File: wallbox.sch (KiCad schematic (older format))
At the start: 36 parts, among them J1 From Transformer, J2 To Wallbox, J3 To Microcontroller, Q1 BC547, Q2 BC547, Q3 BC547, U1 KA78R33, U2 LM7805CT, U3 TPC817MC, U4 TPC817MC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

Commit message: Misc tweaks
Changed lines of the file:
@@
 LIBS:transf
 LIBS:Logic_74xx
+LIBS:ESP8266
 LIBS:wallbox-cache
 EELAYER 25 0
@@
 $EndComp
 Wire Wire Line
-	1700 1300 9250 1300
-Wire Wire Line
-	1700 1700 7950 1700
-Wire Wire Line
-	3200 2200 3200 2850
+	1700 1300 2900 1300
+Wire Wire Line
+	2900 1300 9250 1300
+Wire Wire Line
+	1700 1700 2050 1700
+Wire Wire Line
+	2050 1700 4700 1700
+Wire Wire Line
+	4700 1700 7950 1700
+Wire Wire Line
+	3200 2200 3200 2700
+Wire Wire Line
+	3200 2700 3200 2850
 Wire Wire Line
 	3200 2850 2500 2850
@@
 	2600 2200 2450 2200
 Wire Wire Line
-	2450 2200 2450 4050
+	2450 2200 2450 2700
+Wire Wire Line
+	2450 2700 2450 3450
+Wire Wire Line
+	2450 3450 2450 4050
 Wire Wire Line
 	2450 3450 2900 3450
@@
 Connection ~ 2900 3450
 Wire Wire Line
-	5400 2100 5950 2100
-Wire Wire Line
-	6750 2100 8050 2100
-Wire Wire Line
-	1700 1500 5100 1500
+	5400 2100 5600 2100
+Wire Wire Line
+	5600 2100 5950 2100
+Wire Wire Line
+	6750 2100 7000 2100
+Wire Wire Line
+	7000 2100 7400 2100
+Wire Wire Line
+	7400 2100 8050 2100
+Wire Wire Line
+	1700 1500 1900 1500
+Wire Wire Line
+	1900 1500 5100 1500
 Wire Wire Line
 	7950 1700 7950 1500
 Wire Wire Line
-	7950 1500 9250 1500
+	7950 1500 8950 1500
+Wire Wire Line
+	8950 1500 9250 1500
 Wire Wire Line
 	5400 2100 5400 2200
@@
 	5400 2600 5400 2500
 Wire Wire Line
-	5400 2500 7950 2500
+	5400 2500 5600 2500
+Wire Wire Line
+	5600 2500 5950 2500
+Wire Wire Line
+	5950 2500 6350 2500
+Wire Wire Line
+	6350 2500 6750 2500
+Wire Wire Line
+	6750 2500 7000 2500
+Wire Wire Line
+	7000 2500 7400 2500
+Wire Wire Line
+	7400 2500 7950 2500
 Wire Wire Line
 	5600 2450 5600 2500
@@
 	2650 3600 2650 3850
 Wire Wire Line
-	3250 3850 3600 3850
+	3250 3850 3450 3850
+Wire Wire Line
+	3450 3850 3600 3850
 Wire Wire Line
 	3450 3850 3450 3800
@@
 Connection ~ 3450 3850
 Wire Wire Line
-	3900 3850 4000 3850
+	3900 3850 3950 3850
+Wire Wire Line
+	3950 3850 4000 3850
 Wire Wire Line
 	3950 3900 3950 3850
@@
 	3950 4200 3950 4250
 Wire Wire Line
-	750  2750 750  4300
+	750  2750 750  3100
+Wire Wire Line
+	750  3100 750  3450
+Wire Wire Line
+	750  3450 750  3800
+Wire Wire Line
+	750  3800 750  4150
+Wire Wire Line
+	750  4150 750  4300
 Connection ~ 750  3100
 Connection ~ 750  3450
@@
 	7550 1850 4650 1850
 Wire Wire Line
-	4600 3850 4750 3850
-Wire Wire Line
-	4750 3850 4750 4500
-Wire Wire Line
-	4750 4500 3700 4500
-Wire Wire Line
-	3700 4500 3700 6250
-Wire Wire Line
-	3300 6250 3300 5950
-Wire Wire Line
-	3300 5950 3050 5950
-Wire Wire Line
-	3500 6250 3500 6050
-Wire Wire Line
-	3500 6050 3050 6050
+	4600 3850 4800 3850
+Wire Wire Line
+	4800 3850 4800 4550
+Wire Wire Line
+	4800 4550 3700 4550
+Wire Wire Line
+	3700 4550 3700 6250
 Wire Wire Line
 	8300 3250 7600 3250
@@
 	8050 5650 8300 5650
 Wire Wire Line
-	8050 2100 8050 5650
+	8050 2100 8050 3050
+Wire Wire Line
+	8050 3050 8050 3850
+Wire Wire Line
+	8050 3850 8050 3950
+Wire Wire Line
+	8050 3950 8050 4750
+Wire Wire Line
+	8050 4750 8050 4850
+Wire Wire Line
+	8050 4850 8050 5650
 Wire Wire Line
 	8300 3850 8050 3850
@@
 	7950 5550 7600 5550
 Wire Wire Line
-	7950 2500 7950 5550
+	7950 2500 7950 3750
+Wire Wire Line
+	7950 3750 7950 4650
+Wire Wire Line
+	7950 4650 7950 5550
 Wire Wire Line
 	7600 4650 7950 4650
@@
 	9800 5050 9800 2600
 Wire Wire Line
-	8700 5050 9800 5050
+	8700 5050 8800 5050
+Wire Wire Line
+	8800 5050 9800 5050
 Wire Wire Line
 	9250 1900 9150 1900
@@
 	9700 4150 9700 2700
 Wire Wire Line
-	8700 4150 9700 4150
+	8700 4150 8800 4150
+Wire Wire Line
+	8800 4150 9700 4150
 Wire Wire Line
 	9250 1700 9050 1700
@@
 	9600 3250 9600 2800
 Wire Wire Line
-	8700 3250 9600 3250
+	8700 3250 8800 3250
+Wire Wire Line
+	8800 3250 9600 3250
 Connection ~ 8800 3250
 Connection ~ 8800 4150
@@
 	8950 2900 9500 2900
 Wire Wire Line
-	9500 5650 9500 2900
-Wire Wire Line
-	8700 5650 9500 5650
+	9500 5650 9500 4750
+Wire Wire Line
+	9500 4750 9500 3850
+Wire Wire Line
+	9500 3850 9500 2900
+Wire Wire Line
+	8700 5650 8800 5650
+Wire Wire Line
+	8800 5650 9500 5650
 Connection ~ 8950 1500
 Wire Wire Line
-	8700 4750 9500 4750
+	8700 4750 8800 4750
+Wire Wire Line
+	8800 4750 9500 4750
 Connection ~ 9500 4750
 Wire Wire Line
-	8700 3850 9500 3850
+	8700 3850 8800 3850
+Wire Wire Line
+	8800 3850 9500 3850
 Connection ~ 9500 3850
 Connection ~ 8800 3850
@@
 Text Notes 950  6000 0    60   ~ 0
 Tie-down\nand power
+Wire Wire Line
+	3500 6250 3500 6050
+Wire Wire Line
+	3300 6250 3300 5950
+Wire Wire Line
+	3500 6050 3050 6050
+Wire Wire Line
+	3300 5950 3050 5950
 $EndSCHEMATC

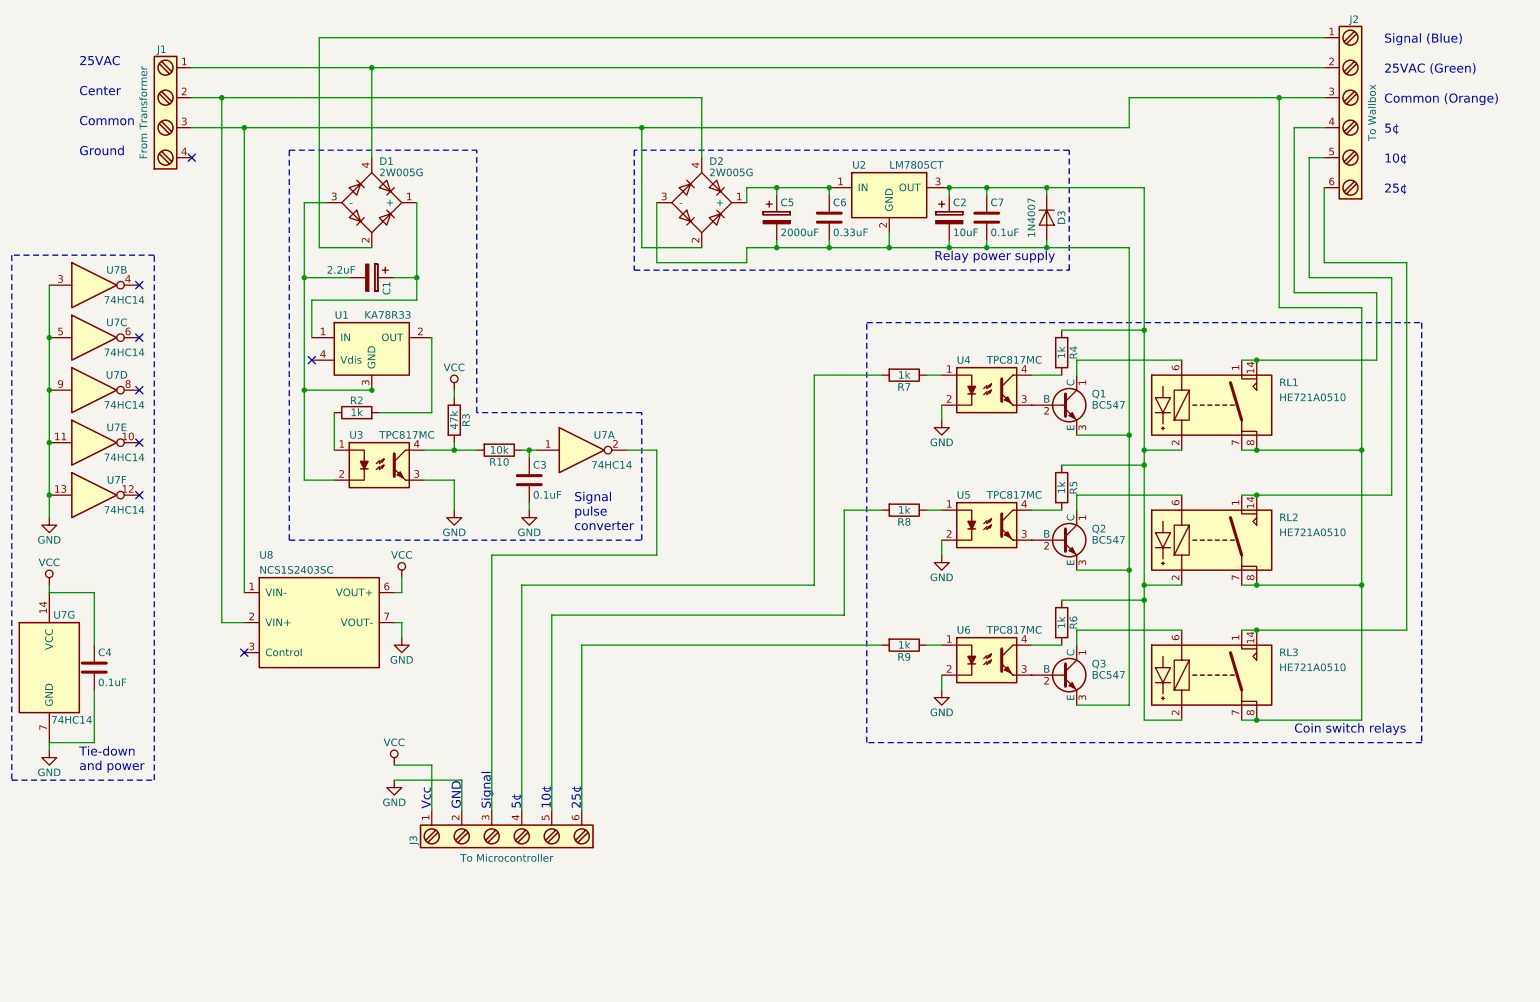
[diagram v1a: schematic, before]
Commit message: Schematic component details filled in
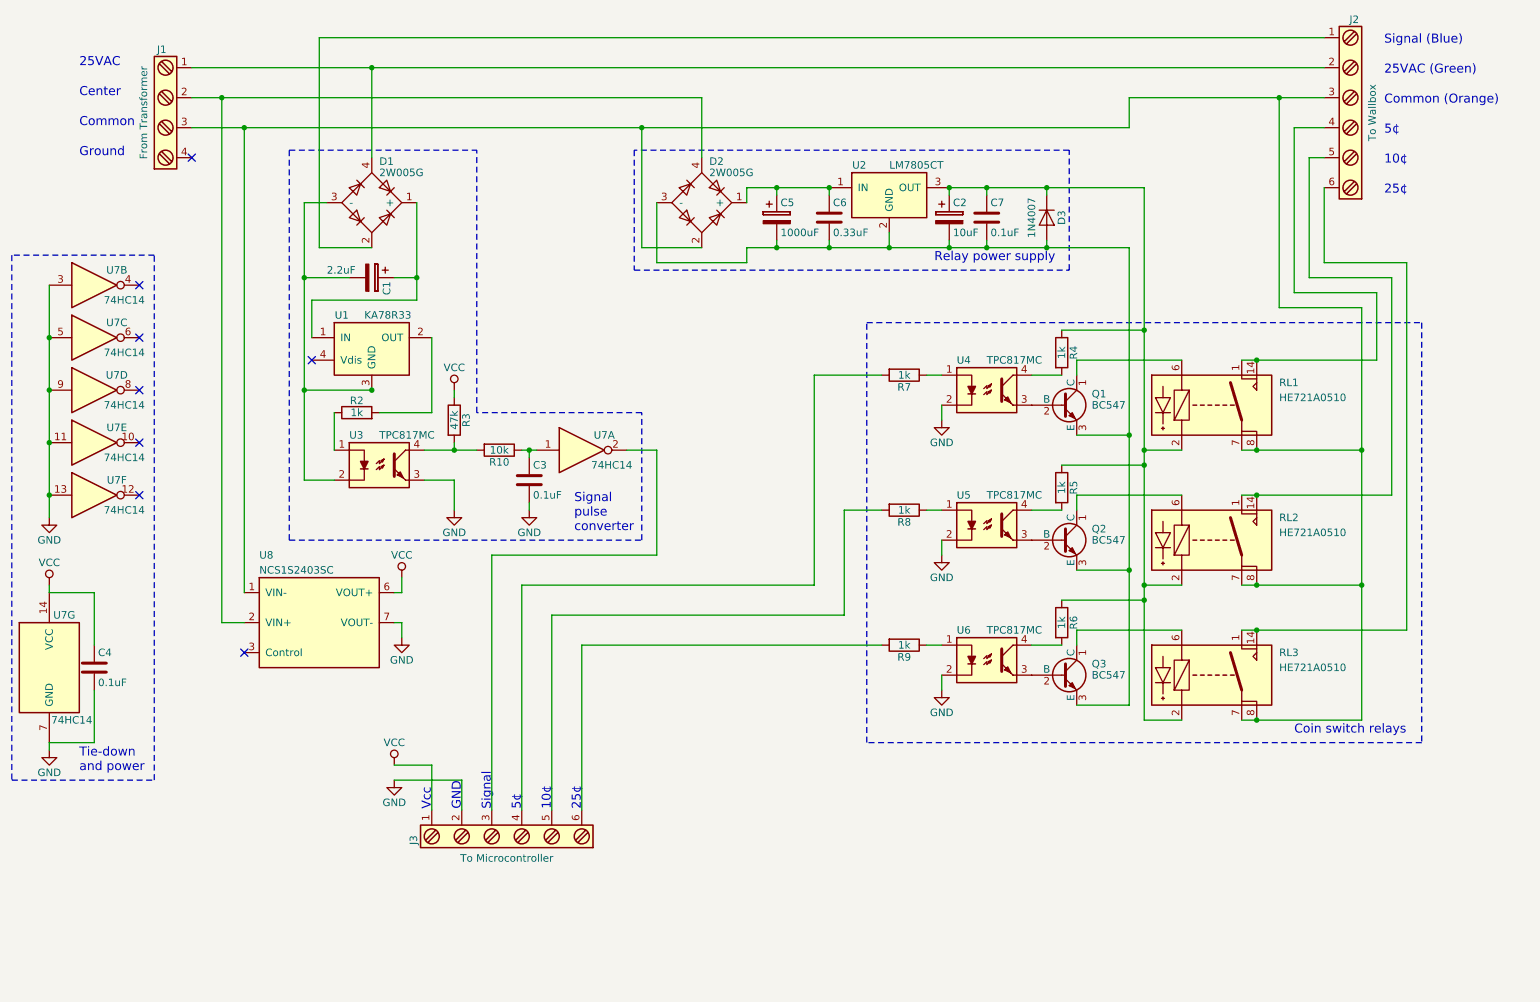
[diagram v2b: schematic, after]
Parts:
- C1: footprint Capacitors_THT:CP_Radial_D10.0mm_P2.50mm -> Capacitors_THT:CP_Radial_D4.0mm_P1.50mm; Description (none) -> CAP ALUM 2.2UF 20% 50V RADIAL
- C2: footprint Capacitors_THT:CP_Radial_D10.0mm_P5.00mm -> Capacitors_THT:CP_Radial_D4.0mm_P1.50mm; Description (none) -> CAP ALUM 10UF 20% 25V RADIAL
- C3, C4: Description (none) -> CAP CER 0.1UF 50V X7R RADIAL
- C5: value 2000uF -> 1000uF; footprint (none) -> Capacitors_THT:CP_Radial_D16.0mm_P7.50mm; Description (none) -> CAP ALUM 1000UF 20% 50V RADIAL
- C6: footprint (none) -> Capacitors_THT:C_Disc_D6.0mm_W2.5mm_P5.00mm; Description (none) -> CAP CER 0.33UF 50V X8L RADIAL
- C7: footprint (none) -> Capacitors_THT:C_Disc_D5.0mm_W2.5mm_P5.00mm; Description (none) -> CAP CER 0.1UF 50V X7R RADIAL
- D1, D2: Description (none) -> DIODE BRIDGE 2A 50V 1PH WOG
- D3: footprint (none) -> Diodes_THT:D_DO-41_SOD81_P12.70mm_Horizontal; Description (none) -> DIODE GEN PURP 1KV 1A DO41
- J1: footprint (none) -> Connectors_Terminal_Blocks:TerminalBlock_Pheonix_MKDS1.5-4pol
- J2, J3: footprint Connectors_Terminal_Blocks:TerminalBlock_Pheonix_PT-3.5mm_6pol -> Connectors_Terminal_Blocks:TerminalBlock_Pheonix_MKDS1.5-6pol
- Q1, Q2, Q3: Description (none) -> TRANS NPN 45V 0.1A TO-92
- R10: footprint Resistors_THT:R_Axial_DIN0204_L3.6mm_D1.6mm_P5.08mm_Horizontal -> Resistors_THT:R_Axial_DIN0207_L6.3mm_D2.5mm_P10.16mm_Horizontal; Description (none) -> RES 10K OHM 1/4W 5% AXIAL
- R2, R4, R5, R6, R7, R8, R9: footprint Resistors_THT:R_Axial_DIN0204_L3.6mm_D1.6mm_P5.08mm_Horizontal -> Resistors_THT:R_Axial_DIN0207_L6.3mm_D2.5mm_P10.16mm_Horizontal; Description (none) -> RES 1K OHM 1/4W 5% AXIAL
- R3: footprint Resistors_THT:R_Axial_DIN0204_L3.6mm_D1.6mm_P5.08mm_Horizontal -> Resistors_THT:R_Axial_DIN0207_L6.3mm_D2.5mm_P10.16mm_Horizontal; Description (none) -> RES 47K OHM 1/4W 5% AXIAL
- RL1, RL2, RL3: Description (none) -> RELAY REED SPST 500MA 5V
- U1: Description (none) -> IC REG LINEAR 3.3V 1A TO220F-4L
- U2: Description (none) -> IC REG LINEAR 5V 1A TO220AB
- U3, U4, U5, U6: footprint Housings_DIP:DIP-4_W7.62mm -> Housings_DIP:DIP-4_W7.62mm_LongPads; Description (none) -> OPTOISO 5KV TRANS DIP-4M
- U7: footprint (none) -> Housings_DIP:DIP-14_W7.62mm_LongPads; Description (none) -> IC HEX SCHMITT-TRIG INV 14-DIP
- U7: footprint (none) -> Housings_DIP:DIP-14_W7.62mm_LongPads
- U8: footprint (none) -> wallbox-footprints:DCDC-Conv_muRata_NCSxxxxSC; Description (none) -> DC/DC CONVERTER 3.3V 1W

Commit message: Updated capacitors, added zener, added DC-DC input components
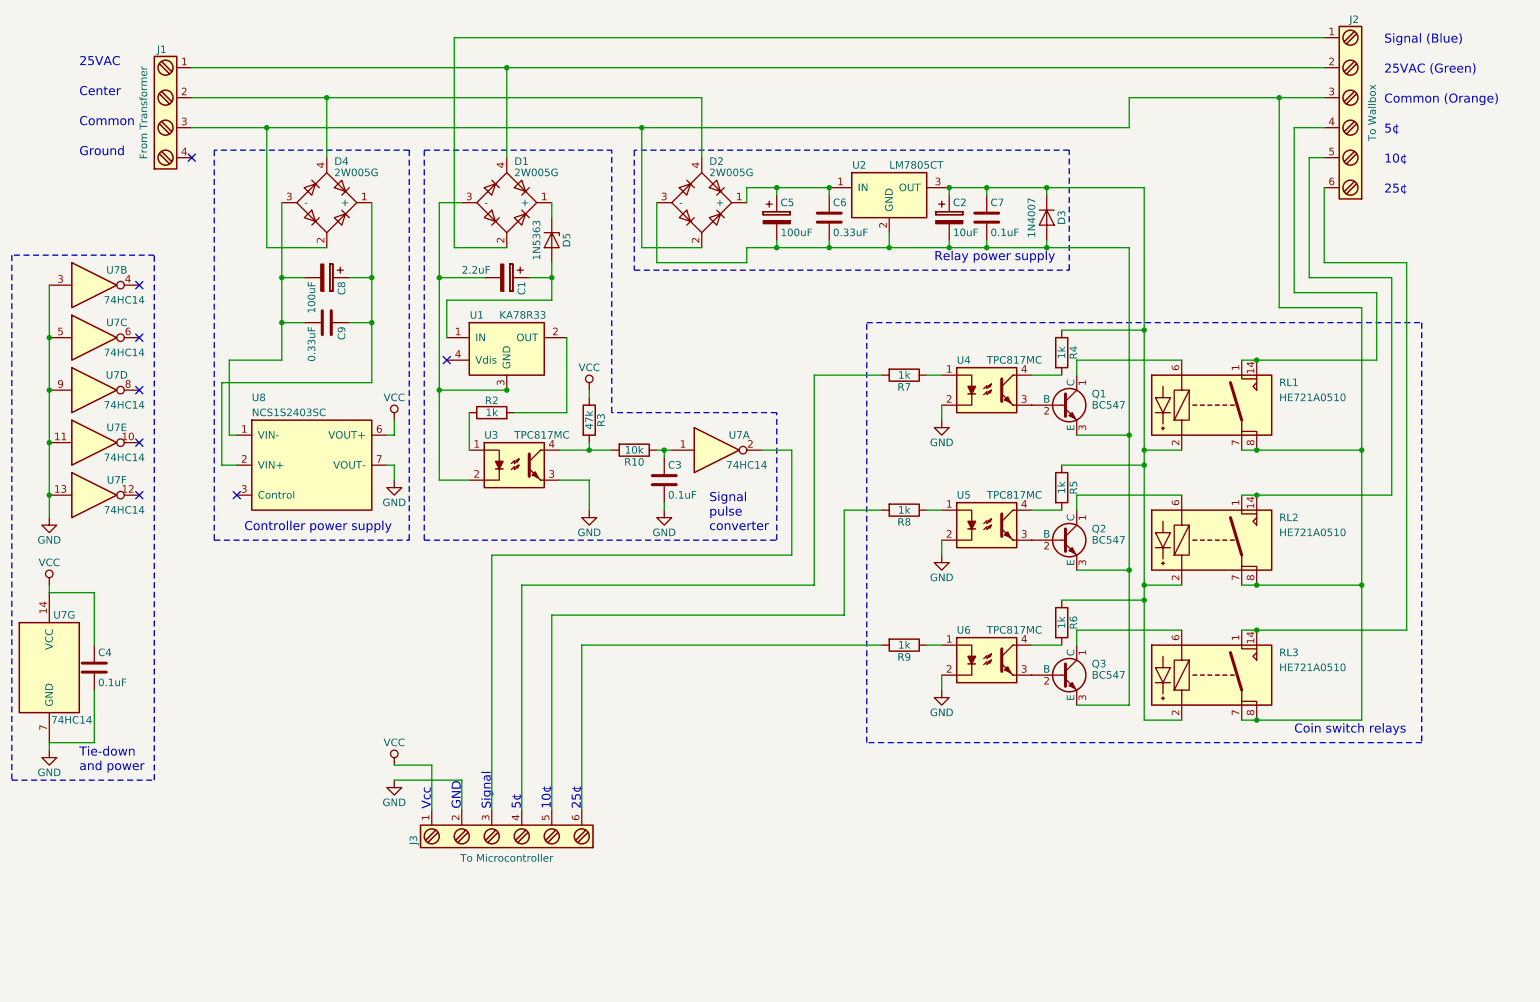
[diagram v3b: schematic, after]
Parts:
- added C8: 100uF, Capacitors_THT:CP_Radial_D8.0mm_P3.50mm, symbol CP
- added C9: 0.33uF, Capacitors_THT:C_Disc_D6.0mm_W2.5mm_P5.00mm, symbol C
- added D4: 2W005G, wallbox-footprints:D-BRIDGE-WOG, symbol 2W005G
- added D5: 1N5363, Diodes_THT:D_DO-41_SOD81_P12.70mm_Horizontal, symbol D_Zener
- C1, C2: footprint Capacitors_THT:CP_Radial_D4.0mm_P1.50mm -> Capacitors_THT:CP_Radial_D5.0mm_P2.00mm
- C5: value 1000uF -> 100uF; footprint Capacitors_THT:CP_Radial_D16.0mm_P7.50mm -> Capacitors_THT:CP_Radial_D8.0mm_P3.50mm; Description CAP ALUM 1000UF 20% 50V RADIAL -> CAP ALUM 100UF 20% 50V RADIAL
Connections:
- net at D2.2, J1.3 (Common), J2.3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: now also D4.2; no longer U8.1 (VIN-)
- net at C1.1, U1.1 (IN): now also D5.2 (A); no longer D1.1 (+)
- net at D2.4, J1.2 (Center): now also D4.4; no longer U8.2 (VIN+)
- new net: D1.1 (+), D5.1 (K)
- new net: C8.1, C9.1, D4.1 (+), U8.2 (VIN+)
- new net: C8.2, C9.2, D4.3 (-), U8.1 (VIN-)
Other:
- note added: "Controller power supply"
- moved on the sheet: C1, C3, D1, R10, R2, R3, U1, U3, U7A, U8

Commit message: Filled in screw terminal component details
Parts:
- J1: Description (none) -> CONN TERM BLOCK 4POS 5MM PCB
- J2: Description (none) -> CONN TERM BLOCK 6POS 5MM PCB
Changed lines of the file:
@@
 F 1 "To Wallbox" V 9300 1600 50  0000 C TNN
 F 2 "Connectors_Terminal_Blocks:TerminalBlock_Pheonix_MKDS1.5-6pol" H 9450 975 50  0001 C CNN
-F 3 "" H 9425 2000 50  0001 C CNN
+F 3 "https://media.digikey.com/pdf/Data%20Sheets/Phoenix%20Contact%20PDFs/1729050.pdf" H 9425 2000 50  0001 C CNN
+F 4 "CONN TERM BLOCK 6POS 5MM PCB" H 9450 1600 60  0001 C CNN "Description"
 	1    9450 1600
 	-1   0    0    -1
@@
 F 1 "From Transformer" V 1350 1600 50  0000 C TNN
 F 2 "Connectors_Terminal_Blocks:TerminalBlock_Pheonix_MKDS1.5-4pol" H 1500 1175 50  0001 C CNN
-F 3 "" H 1475 1800 50  0001 C CNN
+F 3 "https://media.digikey.com/pdf/Data%20Sheets/Phoenix%20Contact%20PDFs/1729034.pdf" H 1475 1800 50  0001 C CNN
+F 4 "CONN TERM BLOCK 4POS 5MM PCB" H 1500 1600 60  0001 C CNN "Description"
 	1    1500 1600
 	1    0    0    -1
